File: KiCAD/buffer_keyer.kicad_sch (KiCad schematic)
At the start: 65 parts, among them J1 Conn_01x02_Pin, J13 Conn_01x05, J2 Conn_01x02_Pin, J3 Conn_01x02_Pin, T1 2N3906, T2 2N3906, U3 MC1496, U4 MCP4921, U6 LM7171xIN, U7 LM7171xIN, U8 MCP4728

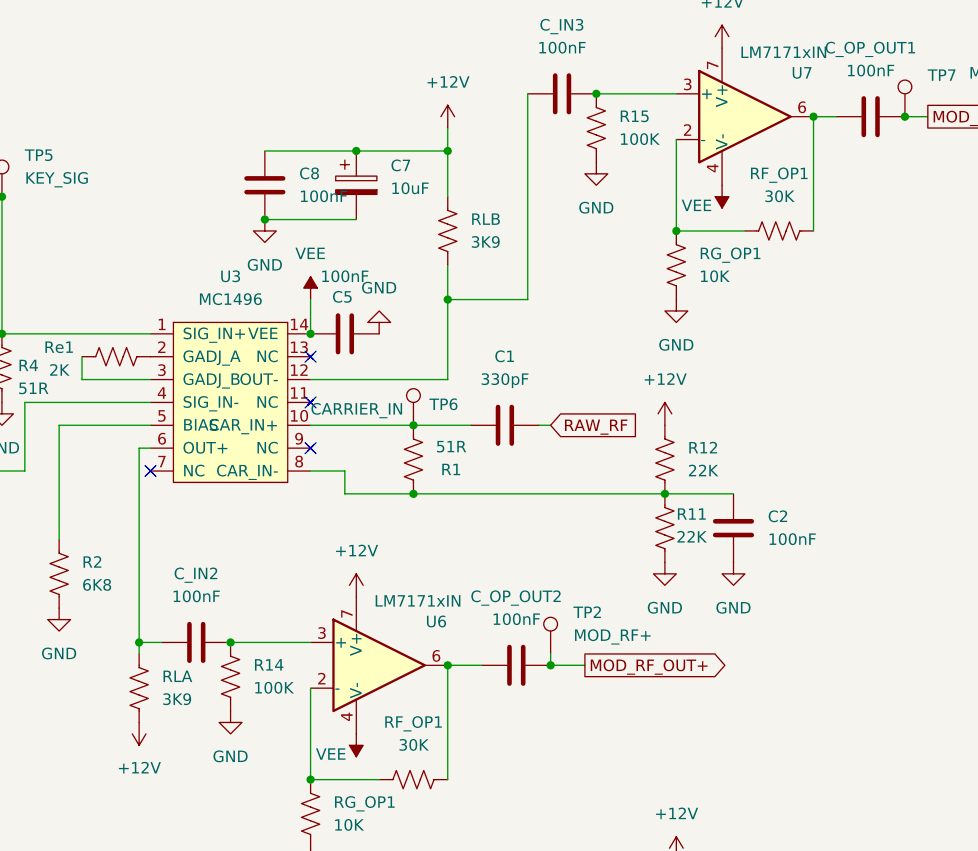
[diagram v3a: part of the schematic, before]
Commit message: buffer_keyer: annotate RLA + break RG_OP1/RF_OP1 duplicate pair
- RLA -> RLA1 (3K9 load resistor at 177.80, 95.25 -- adds numeric suffix)
- RG_OP1 at (237.49, 48.26) -> RG_OP2
- RF_OP1 at (248.92, 44.45) -> RF_OP2
  (second op-amp's gain-set + feedback pair; first pair around U6 LM7171
  keeps the OP1 name)

Resolves the three real ERC bugs from today's second pass. Remaining
21 errors are all in the known-non-issue plateau (U17 unused P-pins,
U17 A0-A2 hardware jumpers, U1 STEMMA-cabled GND, U2/U9 power-output
pin-type quirk).

Co-Authored-By: Claude Opus 4.7 (1M context) <noreply@anthropic.com>
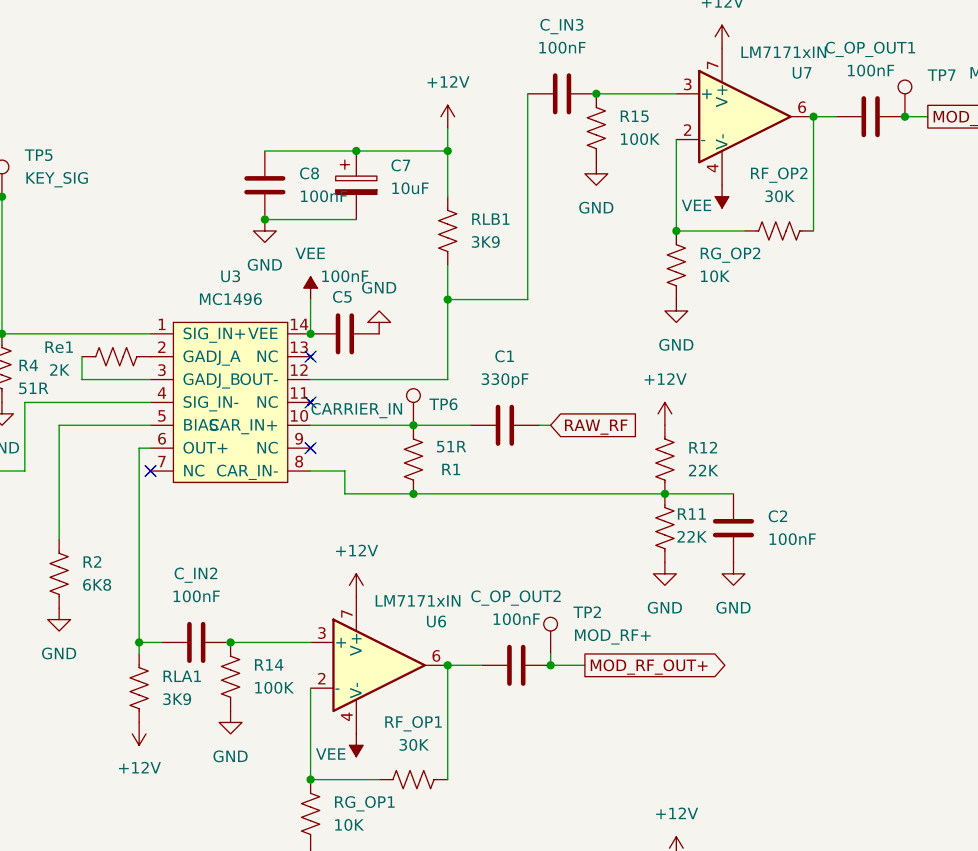
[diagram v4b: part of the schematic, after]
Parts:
- renumbered RF_OP1 to RF_OP2, RG_OP1 to RG_OP2, RLA to RLA1, RLB to RLB1
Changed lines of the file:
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@@
 		(dnp no)
 		(fields_autoplaced yes)
-		(property "Reference" "RLA"
+		(property "Reference" "RLA1"
 			(at 180.34 93.9799 0)
 			(show_name no)
@@
 			(project "KiCAD"
 				(path "/d3de40b8-856b-4fbd-829c-f45ffcd55742/9b3a5939-c591-4389-8331-709ea54f36b7"
-					(reference "RLA")
+					(reference "RLA1")
 					(unit 1)
 				)
@@
 		(dnp no)
 		(fields_autoplaced yes)
-		(property "Reference" "RG_OP1"
+		(property "Reference" "RG_OP2"
 			(at 240.03 46.9899 0)
 			(show_name no)
@@
 			(project "KiCAD"
 				(path "/d3de40b8-856b-4fbd-829c-f45ffcd55742/9b3a5939-c591-4389-8331-709ea54f36b7"
-					(reference "RG_OP1")
+					(reference "RG_OP2")
 					(unit 1)
 				)
@@
 		(dnp no)
 		(fields_autoplaced yes)
-		(property "Reference" "RF_OP1"
+		(property "Reference" "RF_OP2"
 			(at 248.92 38.1 90)
 			(show_name no)
@@
 			(project "KiCAD"
 				(path "/d3de40b8-856b-4fbd-829c-f45ffcd55742/9b3a5939-c591-4389-8331-709ea54f36b7"
-					(reference "RF_OP1")
+					(reference "RF_OP2")
 					(unit 1)
 				)
@@
 		(dnp no)
 		(fields_autoplaced yes)
-		(property "Reference" "RLB"
+		(property "Reference" "RLB1"
 			(at 214.63 43.1799 0)
 			(show_name no)
@@
 			(project "KiCAD"
 				(path "/d3de40b8-856b-4fbd-829c-f45ffcd55742/9b3a5939-c591-4389-8331-709ea54f36b7"
-					(reference "RLB")
+					(reference "RLB1")
 					(unit 1)
 				)

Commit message: kicad: exclude U2 (Metro) from PCB + fix J1/J2/J3 footprints
- U2 Metro ESP32-S3: on_board, in_bom, in_pos_files all set to no.
  Metro sits above the PCB on the Adafruit Wingshield -- it must not be
  imported to the board or included in BOM/pick-and-place. Silences the
  "Cannot add U2 (no footprint assigned)" error from Update PCB from
  Schematic.
- buffer_keyer J1, J2, J3: replace stale
  TerminalBlock_Phoenix_MKDS-1,5-10-5.08_1x10 footprint (10-position TB
  wrong for 2-pin conns) with the standard
  Connector_PinHeader_2.54mm:PinHeader_1x02_P2.54mm_Vertical used
  everywhere else in the project.

Co-Authored-By: Claude Opus 4.7 (1M context) <noreply@anthropic.com>
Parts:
- J1, J2, J3: footprint TerminalBlock_Phoenix:TerminalBlock_Phoenix_MKDS-1,5-10-5.08_1x10_P5.08mm_Horizontal -> Connector_PinHeader_2.54mm:PinHeader_1x02_P2.54mm_Vertical
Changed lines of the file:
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@@
 			)
 		)
-		(property "Footprint" "TerminalBlock_Phoenix:TerminalBlock_Phoenix_MKDS-1,5-10-5.08_1x10_P5.08mm_Horizontal"
+		(property "Footprint" "Connector_PinHeader_2.54mm:PinHeader_1x02_P2.54mm_Vertical"
 			(at 21.59 60.96 0)
 			(hide yes)
@@
 			)
 		)
-		(property "Footprint" "TerminalBlock_Phoenix:TerminalBlock_Phoenix_MKDS-1,5-10-5.08_1x10_P5.08mm_Horizontal"
+		(property "Footprint" "Connector_PinHeader_2.54mm:PinHeader_1x02_P2.54mm_Vertical"
 			(at 21.59 101.6 0)
 			(hide yes)
@@
 			)
 		)
-		(property "Footprint" "TerminalBlock_Phoenix:TerminalBlock_Phoenix_MKDS-1,5-10-5.08_1x10_P5.08mm_Horizontal"
+		(property "Footprint" "Connector_PinHeader_2.54mm:PinHeader_1x02_P2.54mm_Vertical"
 			(at 21.59 78.74 0)
 			(hide yes)

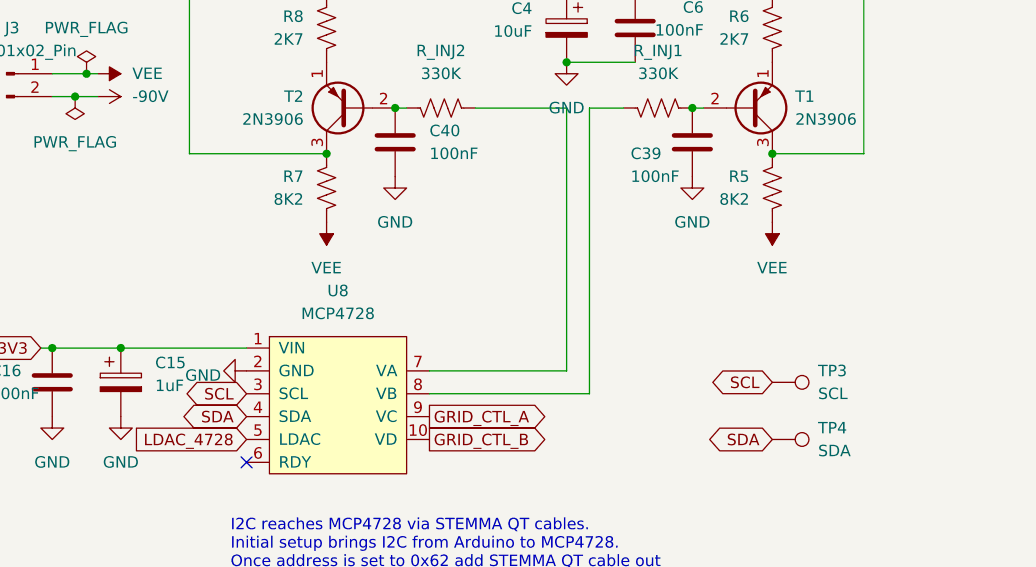
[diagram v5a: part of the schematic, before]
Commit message: kicad: buffer_keyer partial placement + MCP4728 footprint rebuild
- KiCAD.kicad_pcb: initial placement of 19 buffer_keyer parts (MC1496
  keyer, T1/T2 2N3906s, VEE divider R7/R8, LM4040, C4 10uF bulk, R_INJ1
  and adjacent passives) on the 200x150 board alongside the completed
  VFO block. Zero routing yet.
- Adafruit_MCP4728_Breakout.kicad_mod: rebuild for the correct 2 x 6-pin
  physical layout (was 5+5). Top row JP2 = GND VA VB VC VD VCC, bottom
  row JP1 = VCC GND SCL SDA LDAC RDY. Duplicate VCC/GND pads share
  pad numbers (1,2) so they tie to the same nets as the symbol's VIN/GND.
  Silk labels rebuilt as 12 per-pin fp_text items centered on each pin's
  X coordinate for clear placement verification.
- buffer_keyer.kicad_sch: two 100nF VEE-to-GND decoupling caps added at
  T1 and T2.

Co-Authored-By: Claude Opus 4.7 <noreply@anthropic.com>
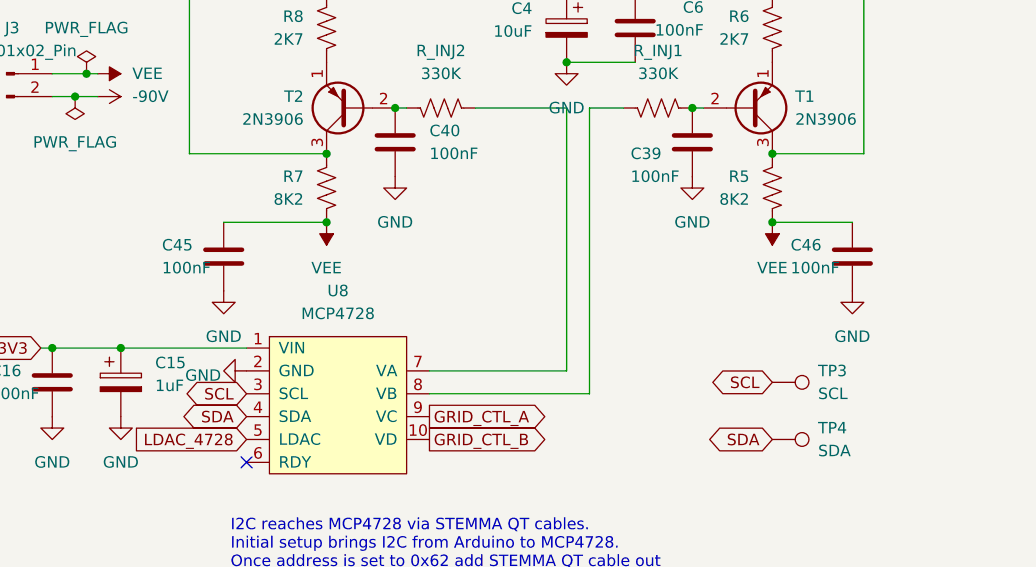
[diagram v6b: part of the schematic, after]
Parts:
- added C45, C46: 100nF, Capacitor_THT:C_Disc_D5.0mm_W2.5mm_P5.00mm, symbol Device:C
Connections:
- net GND: now also C45.2, C46.2
- net VEE: now also C45.1, C46.1

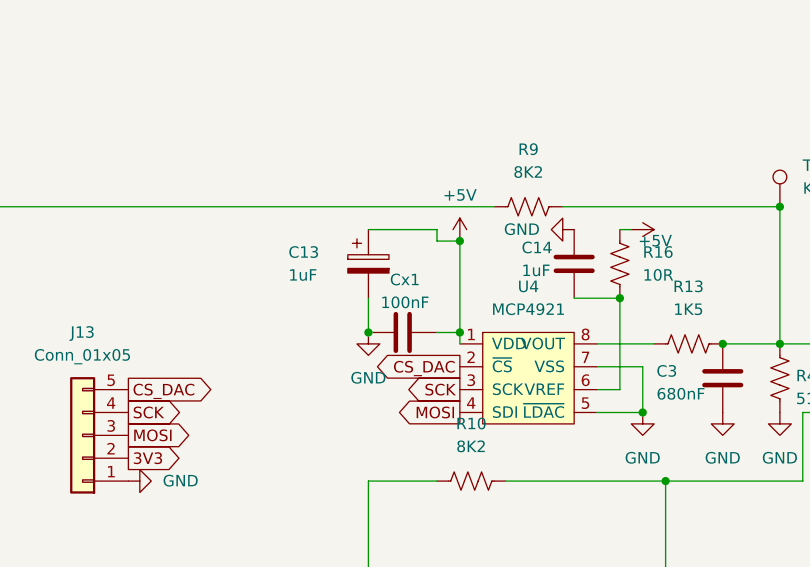
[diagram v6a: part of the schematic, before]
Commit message: docs: two-box construction plan; kicad: ongoing layout + T1/T2 decoupling
- construction.md: new "Electronics-in-a-separate-box strategy" section.
  Control PCB (MC1496 keyer, MCP4921 DAC, Si5351 VFO, MCP4728 DAC,
  Metro ESP32-S3) goes in a small metal box on top of the main chassis;
  MOD_RF_OUT+/- crosses the gap through bulkhead BNCs on both boxes.
  Recommended part Amphenol RF 112404. Documents the signal chain,
  balance/matching requirements for CW carrier suppression, and the
  grounding scheme (both boxes bonded through the coax shield).
- buffer_keyer.kicad_sch: continued edits including the two 100nF
  VEE-to-GND decoupling caps at T1/T2 noted earlier.
- KiCAD.kicad_pcb: ongoing buffer_keyer placement progress.

Co-Authored-By: Claude Opus 4.7 <noreply@anthropic.com>
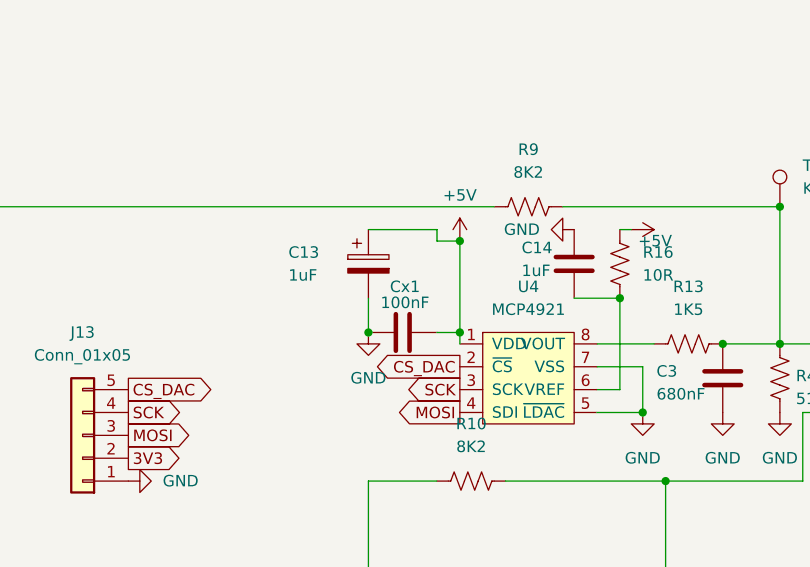
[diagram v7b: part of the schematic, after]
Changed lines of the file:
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@@
 		(dnp no)
 		(property "Reference" "Cx1"
-			(at 120.904 48.768 90)
+			(at 120.904 49.53 90)
 			(show_name no)
 			(do_not_autoplace no)

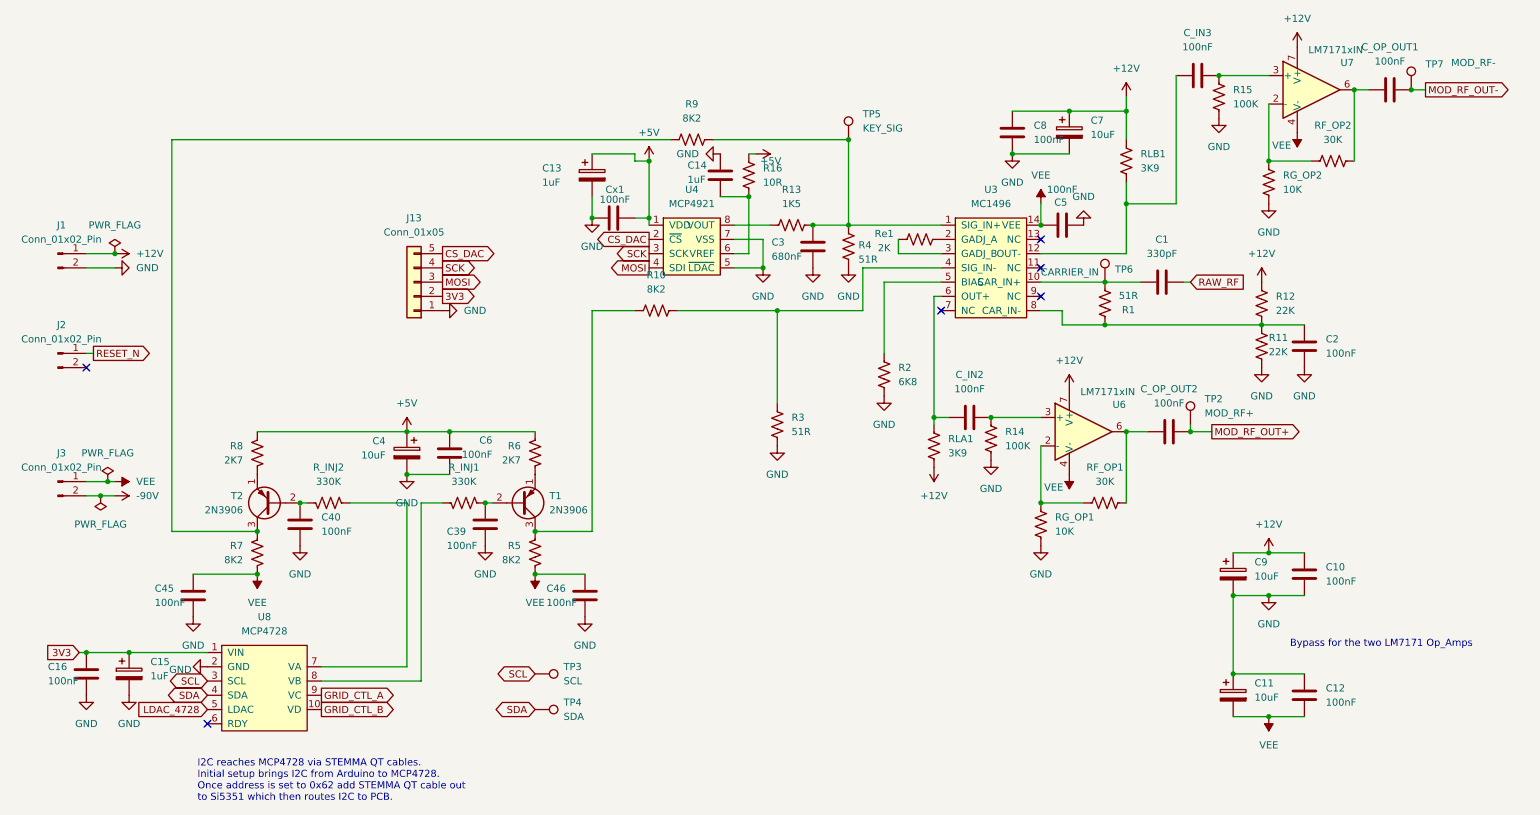
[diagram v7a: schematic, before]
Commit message: kicad: local VEE generator (ICL7660S + L7908) on buffer_keyer
Replaces the external -8V (VEE) supply that previously came in through
J3 with a locally-generated one from the existing +12V rail. Charge-pump
inverts +12V to ~-11V, linear regulator drops to a clean -8V.

Schematic (buffer_keyer.kicad_sch):
- U15: ICL7660S charge pump (new symbol xmitter:ICL7660S_Boost with
  BOOST pin exposed on pin 1, tied to +12V for 35kHz oscillator).
  Package_DIP:DIP-8_W7.62mm.
- U19: L79L08_TO92 fixed -8V negative regulator, TO-92 inline.
  Mirror-x removed so pin numbering (1=GND, 2=VI, 3=VO) matches the
  wiring.
- C48 (10uF pump), C49 (100uF reservoir on charge-pump output), C50
  (10uF regulator output), C51 (100nF HF bypass on VEE output).
- 0.1uF ceramic between +12V and GND close to U15 pin 8 (input
  decoupling per datasheet).
- PWR_FLAG moved from external VEE input to the L7908 output so ERC
  sees the local generator as the source of record.

Symbol library (xmitter.kicad_sym):
- ICL7660S_Boost added. Same electrical layout as the KiCad stock
  ICL7660 except pin 1 exposed as BOOST (was hidden NC). Extended
  rectangle top by 2.54mm to make room.

Still open (deferred): J3 to be removed entirely -- it belongs on the
bias board, with its VEE pin repurposed as GND for the -90V return
path.

Co-Authored-By: Claude Opus 4.7 <noreply@anthropic.com>
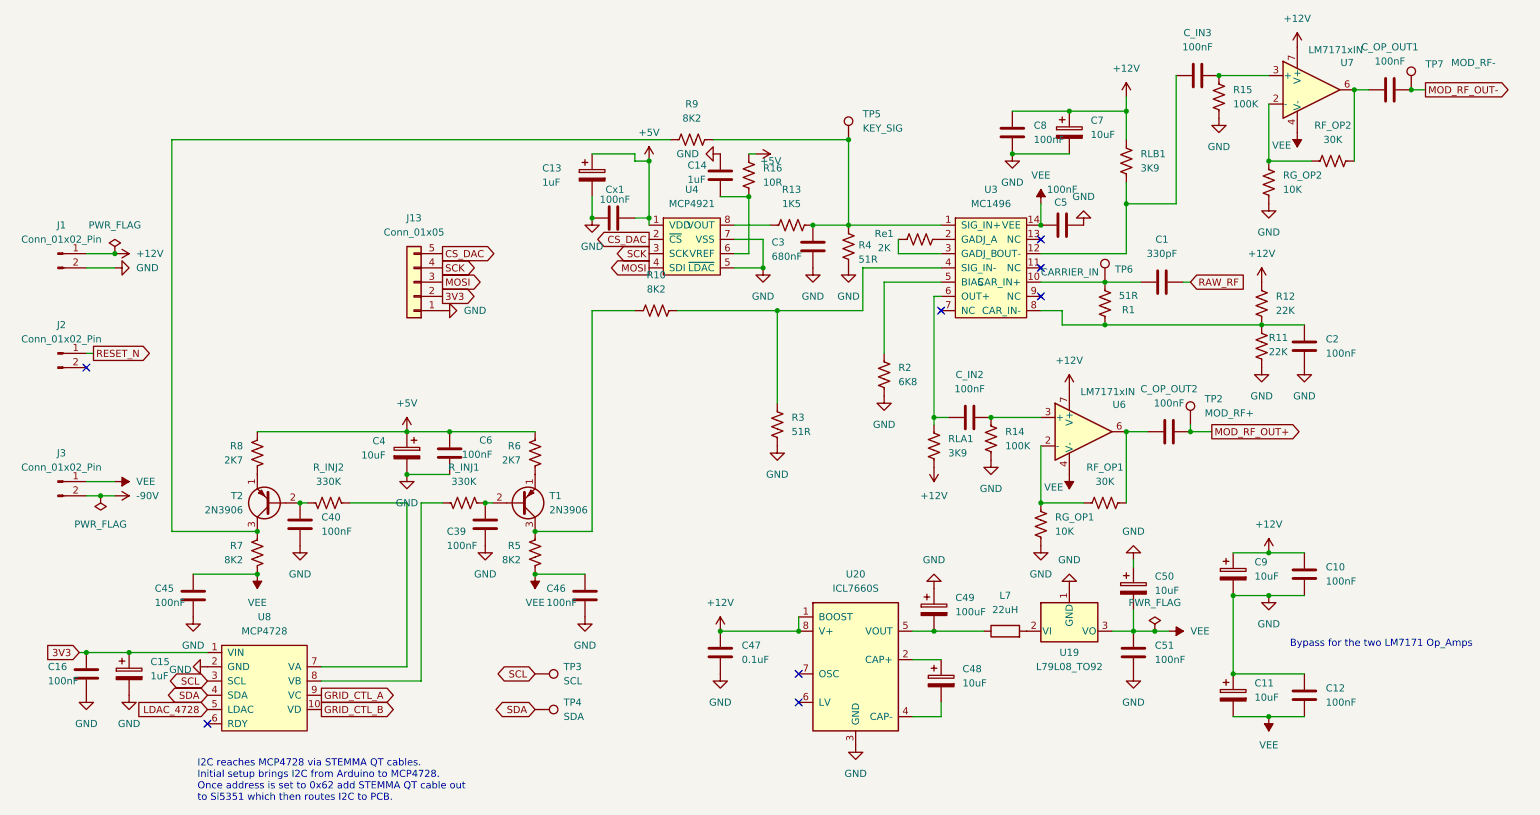
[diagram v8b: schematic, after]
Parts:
- added C47: 0.1uF, symbol Device:C
- added C48, C50: 10uF, symbol Device:C_Polarized
- added C49: 100uF, symbol Device:C_Polarized
- added C51: 100nF, symbol Device:C
- added L7: 22uH, symbol Device:R
- added U19: L79L08_TO92, Package_TO_SOT_THT:TO-92_Inline, symbol Regulator_Linear:L79L08_TO92
- added U20: ICL7660S, Package_DIP:DIP-8_W7.62mm, symbol xmitter:ICL7660S_Boost
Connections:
- net +12V: now also C47.1, U20.1 (BOOST), U20.8 (V+)
- net GND: now also C47.2, C49.1, C50.1, C51.2, U19.1 (GND), U20.3 (GND)
- net VEE: now also C50.2, C51.1, U19.3 (VO)
- new net: L7.2, U19.2 (VI)
- new net: C49.2, L7.1, U20.5 (VOUT)
- new net: C48.1, U20.2 (CAP+)
- new net: C48.2, U20.4 (CAP-)
- no-connect marks 6 -> 8
